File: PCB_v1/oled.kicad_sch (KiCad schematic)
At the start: 17 parts, among them J6 OLED Conn_02x04, SW2 SW_Push, SW3 SW_Push, SW4 SW_Push, SW5 SW_Push, SW6 SW_Push, SW7 SW_Push, U3 SMS05T1G, U4 SMS05T1G

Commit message: added the oscilator
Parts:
- TP3, TP4, TP5, TP6: footprint TestPoint:TestPoint_THTPad_D1.0mm_Drill0.5mm -> TestPoint_THTPad_D0.5mm_Drill0.3mm
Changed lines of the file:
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@@
 	(label "B5"
 		(at 77.47 148.59 0)
+		(fields_autoplaced yes)
 		(effects
 			(font
@@
 	(label "B1"
 		(at 22.86 46.99 0)
+		(fields_autoplaced yes)
 		(effects
 			(font
@@
 	(label "B6"
 		(at 77.47 179.07 0)
+		(fields_autoplaced yes)
 		(effects
 			(font
@@
 	(label "B7"
 		(at 22.86 87.63 0)
+		(fields_autoplaced yes)
 		(effects
 			(font
@@
 	(label "B8"
 		(at 55.88 87.63 0)
+		(fields_autoplaced yes)
 		(effects
 			(font
@@
 	(label "B4"
 		(at 77.47 116.84 0)
+		(fields_autoplaced yes)
 		(effects
 			(font
@@
 	(label "B1"
 		(at 77.47 33.02 0)
+		(fields_autoplaced yes)
 		(effects
 			(font
@@
 	(label "B7"
 		(at 187.96 104.14 0)
+		(fields_autoplaced yes)
 		(effects
 			(font
@@
 	(label "B3"
 		(at 77.47 88.9 0)
+		(fields_autoplaced yes)
 		(effects
 			(font
@@
 	(label "B3"
 		(at 55.88 57.15 0)
+		(fields_autoplaced yes)
 		(effects
 			(font
@@
 	(label "B2"
 		(at 77.47 59.69 0)
+		(fields_autoplaced yes)
 		(effects
 			(font
@@
 	(label "B4"
 		(at 22.86 57.15 0)
+		(fields_autoplaced yes)
 		(effects
 			(font
@@
 	(label "B6"
 		(at 55.88 77.47 0)
+		(fields_autoplaced yes)
 		(effects
 			(font
@@
 	(label "B2"
 		(at 55.88 46.99 0)
+		(fields_autoplaced yes)
 		(effects
 			(font
@@
 	(label "B5"
 		(at 22.86 77.47 0)
+		(fields_autoplaced yes)
 		(effects
 			(font
@@
 	(label "B8"
 		(at 189.23 139.7 0)
+		(fields_autoplaced yes)
 		(effects
 			(font
@@
 		(shape output)
 		(at 104.14 116.84 0)
+		(fields_autoplaced yes)
 		(effects
 			(font
@@
 		(shape input)
 		(at 149.86 49.53 0)
+		(fields_autoplaced yes)
 		(effects
 			(font
@@
 		(shape input)
 		(at 137.16 41.91 180)
+		(fields_autoplaced yes)
 		(effects
 			(font
@@
 		(shape input)
 		(at 137.16 46.99 180)
+		(fields_autoplaced yes)
 		(effects
 			(font
@@
 		(shape output)
 		(at 104.14 59.69 0)
+		(fields_autoplaced yes)
 		(effects
 			(font
@@
 		(shape input)
 		(at 149.86 41.91 0)
+		(fields_autoplaced yes)
 		(effects
 			(font
@@
 		(shape input)
 		(at 149.86 44.45 0)
+		(fields_autoplaced yes)
 		(effects
 			(font
@@
 		(shape output)
 		(at 104.14 88.9 0)
+		(fields_autoplaced yes)
 		(effects
 			(font
@@
 		(shape output)
 		(at 104.14 179.07 0)
+		(fields_autoplaced yes)
 		(effects
 			(font
@@
 		(shape input)
 		(at 137.16 49.53 180)
+		(fields_autoplaced yes)
 		(effects
 			(font
@@
 		(shape input)
 		(at 154.94 73.66 0)
+		(fields_autoplaced yes)
 		(effects
 			(font
@@
 		(shape input)
 		(at 137.16 44.45 180)
+		(fields_autoplaced yes)
 		(effects
 			(font
@@
 		(shape output)
 		(at 104.14 148.59 0)
+		(fields_autoplaced yes)
 		(effects
 			(font
@@
 		(shape input)
 		(at 134.62 73.66 0)
+		(fields_autoplaced yes)
 		(effects
 			(font
@@
 		(shape output)
 		(at 104.14 33.02 0)
+		(fields_autoplaced yes)
 		(effects
 			(font
@@
 		(shape input)
 		(at 149.86 46.99 0)
+		(fields_autoplaced yes)
 		(effects
 			(font
@@
 			)
 		)
-		(property "Footprint" "TestPoint:TestPoint_THTPad_D1.0mm_Drill0.5mm"
+		(property "Footprint" "TestPoint_THTPad_D0.5mm_Drill0.3mm"
 			(at 194.31 144.78 0)
 			(effects
@@
 			)
 		)
-		(property "Footprint" "TestPoint:TestPoint_THTPad_D1.0mm_Drill0.5mm"
+		(property "Footprint" "TestPoint_THTPad_D0.5mm_Drill0.3mm"
 			(at 161.29 134.62 0)
 			(effects
@@
 			)
 		)
-		(property "Footprint" "TestPoint:TestPoint_THTPad_D1.0mm_Drill0.5mm"
+		(property "Footprint" "TestPoint_THTPad_D0.5mm_Drill0.3mm"
 			(at 161.29 100.33 0)
 			(effects
@@
 			)
 		)
-		(property "Footprint" "TestPoint:TestPoint_THTPad_D1.0mm_Drill0.5mm"
+		(property "Footprint" "TestPoint_THTPad_D0.5mm_Drill0.3mm"
 			(at 193.04 109.22 0)
 			(effects

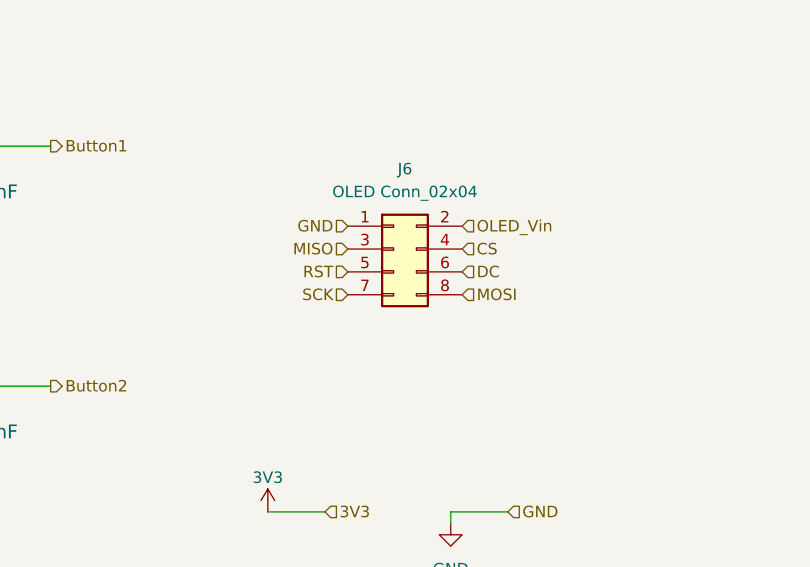
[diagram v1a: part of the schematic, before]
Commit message: push for jtag fix
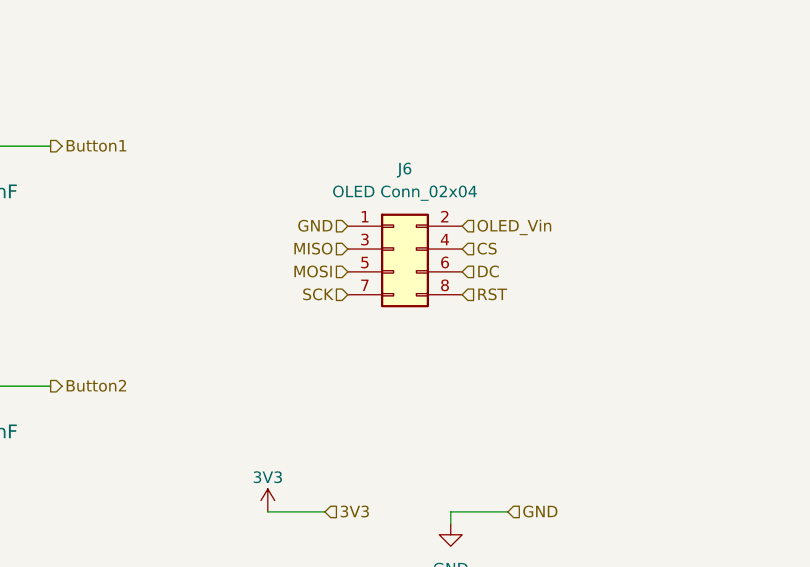
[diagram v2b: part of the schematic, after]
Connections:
- net MOSI: now also J6.5 (Pin_5); no longer J6.8 (Pin_8)
- net RST: now also J6.8 (Pin_8); no longer J6.5 (Pin_5)
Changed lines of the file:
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@@
 	(label "B5"
 		(at 77.47 148.59 0)
-		(fields_autoplaced yes)
 		(effects
 			(font
@@
 	(label "B1"
 		(at 22.86 46.99 0)
-		(fields_autoplaced yes)
 		(effects
 			(font
@@
 	(label "B6"
 		(at 77.47 179.07 0)
-		(fields_autoplaced yes)
 		(effects
 			(font
@@
 	(label "B7"
 		(at 22.86 87.63 0)
-		(fields_autoplaced yes)
 		(effects
 			(font
@@
 	(label "B8"
 		(at 55.88 87.63 0)
-		(fields_autoplaced yes)
 		(effects
 			(font
@@
 	(label "B4"
 		(at 77.47 116.84 0)
-		(fields_autoplaced yes)
 		(effects
 			(font
@@
 	(label "B1"
 		(at 77.47 33.02 0)
-		(fields_autoplaced yes)
 		(effects
 			(font
@@
 	(label "B7"
 		(at 187.96 104.14 0)
-		(fields_autoplaced yes)
 		(effects
 			(font
@@
 	(label "B3"
 		(at 77.47 88.9 0)
-		(fields_autoplaced yes)
 		(effects
 			(font
@@
 	(label "B3"
 		(at 55.88 57.15 0)
-		(fields_autoplaced yes)
 		(effects
 			(font
@@
 	(label "B2"
 		(at 77.47 59.69 0)
-		(fields_autoplaced yes)
 		(effects
 			(font
@@
 	(label "B4"
 		(at 22.86 57.15 0)
-		(fields_autoplaced yes)
 		(effects
 			(font
@@
 	(label "B6"
 		(at 55.88 77.47 0)
-		(fields_autoplaced yes)
 		(effects
 			(font
@@
 	(label "B2"
 		(at 55.88 46.99 0)
-		(fields_autoplaced yes)
 		(effects
 			(font
@@
 	(label "B5"
 		(at 22.86 77.47 0)
-		(fields_autoplaced yes)
 		(effects
 			(font
@@
 	(label "B8"
 		(at 189.23 139.7 0)
-		(fields_autoplaced yes)
 		(effects
 			(font
@@
 		(shape output)
 		(at 104.14 116.84 0)
-		(fields_autoplaced yes)
 		(effects
 			(font
@@
 	(hierarchical_label "MOSI"
 		(shape input)
+		(at 137.16 46.99 180)
+		(effects
+			(font
+				(size 1.27 1.27)
+			)
+			(justify right)
+		)
+	)
+	(hierarchical_label "GND"
+		(shape input)
+		(at 137.16 41.91 180)
+		(effects
+			(font
+				(size 1.27 1.27)
+			)
+			(justify right)
+		)
+	)
+	(hierarchical_label "RST"
+		(shape input)
 		(at 149.86 49.53 0)
-		(fields_autoplaced yes)
-		(effects
-			(font
-				(size 1.27 1.27)
-			)
-			(justify left)
+		(effects
+			(font
+				(size 1.27 1.27)
+			)
+			(justify left)
+		)
+	)
+	(hierarchical_label "Button2"
+		(shape output)
+		(at 104.14 59.69 0)
+		(effects
+			(font
+				(size 1.27 1.27)
+			)
+			(justify left)
+		)
+	)
+	(hierarchical_label "OLED_Vin"
+		(shape input)
+		(at 149.86 41.91 0)
+		(effects
+			(font
+				(size 1.27 1.27)
+			)
+			(justify left)
+		)
+	)
+	(hierarchical_label "CS"
+		(shape input)
+		(at 149.86 44.45 0)
+		(effects
+			(font
+				(size 1.27 1.27)
+			)
+			(justify left)
+		)
+	)
+	(hierarchical_label "Button3"
+		(shape output)
+		(at 104.14 88.9 0)
+		(effects
+			(font
+				(size 1.27 1.27)
+			)
+			(justify left)
+		)
+	)
+	(hierarchical_label "Button6"
+		(shape output)
+		(at 104.14 179.07 0)
+		(effects
+			(font
+				(size 1.27 1.27)
+			)
+			(justify left)
+		)
+	)
+	(hierarchical_label "SCK"
+		(shape input)
+		(at 137.16 49.53 180)
+		(effects
+			(font
+				(size 1.27 1.27)
+			)
+			(justify right)
 		)
 	)
 	(hierarchical_label "GND"
 		(shape input)
-		(at 137.16 41.91 180)
-		(fields_autoplaced yes)
-		(effects
-			(font
-				(size 1.27 1.27)
-			)
-			(justify right)
-		)
-	)
-	(hierarchical_label "RST"
-		(shape input)
-		(at 137.16 46.99 180)
-		(fields_autoplaced yes)
-		(effects
-			(font
-				(size 1.27 1.27)
-			)
-			(justify right)
-		)
-	)
-	(hierarchical_label "Button2"
-		(shape output)
-		(at 104.14 59.69 0)
-		(fields_autoplaced yes)
-		(effects
-			(font
-				(size 1.27 1.27)
-			)
-			(justify left)
-		)
-	)
-	(hierarchical_label "OLED_Vin"
-		(shape input)
-		(at 149.86 41.91 0)
-		(fields_autoplaced yes)
-		(effects
-			(font
-				(size 1.27 1.27)
-			)
-			(justify left)
-		)
-	)
-	(hierarchical_label "CS"
-		(shape input)
-		(at 149.86 44.45 0)
-		(fields_autoplaced yes)
-		(effects
-			(font
-				(size 1.27 1.27)
-			)
-			(justify left)
-		)
-	)
-	(hierarchical_label "Button3"
-		(shape output)
-		(at 104.14 88.9 0)
-		(fields_autoplaced yes)
-		(effects
-			(font
-				(size 1.27 1.27)
-			)
-			(justify left)
-		)
-	)
-	(hierarchical_label "Button6"
-		(shape output)
-		(at 104.14 179.07 0)
-		(fields_autoplaced yes)
-		(effects
-			(font
-				(size 1.27 1.27)
-			)
-			(justify left)
-		)
-	)
-	(hierarchical_label "SCK"
-		(shape input)
-		(at 137.16 49.53 180)
-		(fields_autoplaced yes)
-		(effects
-			(font
-				(size 1.27 1.27)
-			)
-			(justify right)
-		)
-	)
-	(hierarchical_label "GND"
-		(shape input)
 		(at 154.94 73.66 0)
-		(fields_autoplaced yes)
 		(effects
 			(font
@@
 		(shape input)
 		(at 137.16 44.45 180)
-		(fields_autoplaced yes)
 		(effects
 			(font
@@
 		(shape output)
 		(at 104.14 148.59 0)
-		(fields_autoplaced yes)
 		(effects
 			(font
@@
 		(shape input)
 		(at 134.62 73.66 0)
-		(fields_autoplaced yes)
 		(effects
 			(font
@@
 		(shape output)
 		(at 104.14 33.02 0)
-		(fields_autoplaced yes)
 		(effects
 			(font
@@
 		(shape input)
 		(at 149.86 46.99 0)
-		(fields_autoplaced yes)
-		(effects
-			(font
+		(effects
+			(font

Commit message: before major move
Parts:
- TP3, TP4, TP5, TP6: footprint TestPoint_THTPad_D0.5mm_Drill0.3mm -> TestPoint_THTPad_D0.8mm_Drill0.4mm
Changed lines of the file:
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@@
 			)
 		)
-		(property "Footprint" "TestPoint_THTPad_D0.5mm_Drill0.3mm"
+		(property "Footprint" "TestPoint_THTPad_D0.8mm_Drill0.4mm"
 			(at 194.31 144.78 0)
 			(effects
@@
 			)
 		)
-		(property "Footprint" "TestPoint_THTPad_D0.5mm_Drill0.3mm"
+		(property "Footprint" "TestPoint_THTPad_D0.8mm_Drill0.4mm"
 			(at 161.29 134.62 0)
 			(effects
@@
 			)
 		)
-		(property "Footprint" "TestPoint_THTPad_D0.5mm_Drill0.3mm"
+		(property "Footprint" "TestPoint_THTPad_D0.8mm_Drill0.4mm"
 			(at 161.29 100.33 0)
 			(effects
@@
 			)
 		)
-		(property "Footprint" "TestPoint_THTPad_D0.5mm_Drill0.3mm"
+		(property "Footprint" "TestPoint_THTPad_D0.8mm_Drill0.4mm"
 			(at 193.04 109.22 0)
 			(effects

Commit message: Placement done
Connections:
- net B1: now also U3.6; no longer U3.4
- net B2: now also U3.4; no longer U3.3
- net B3: now also U3.3; no longer U3.1
- net B4: now also U3.1; no longer U3.6
- net CS: now also J6.7 (Pin_7); no longer J6.4 (Pin_4)
- net GND: now also J6.2 (Pin_2); no longer J6.1 (Pin_1)
- net MOSI: now also J6.1 (Pin_1); no longer J6.5 (Pin_5)
- net OLED_Vin: now also J6.4 (Pin_4); no longer J6.2 (Pin_2)
- net SCK: now also J6.5 (Pin_5); no longer J6.7 (Pin_7)
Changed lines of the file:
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@@
+	(wire
+		(pts
+			(xy 151.13 46.99) (xy 149.86 46.99)
+		)
+		(stroke
+			(width 0)
+			(type default)
+		)
+	)
 	(wire
 		(pts
@@
 	(wire
 		(pts
+			(xy 19.05 57.15) (xy 22.86 57.15)
+		)
+		(stroke
+			(width 0)
+			(type default)
+		)
+	)
+	(wire
+		(pts
 			(xy 77.47 148.59) (xy 80.01 148.59)
 		)
@@
 	(wire
 		(pts
+			(xy 57.15 46.99) (xy 55.88 46.99)
+		)
+		(stroke
+			(width 0)
+			(type default)
+		)
+	)
+	(wire
+		(pts
+			(xy 151.13 44.45) (xy 149.86 44.45)
+		)
+		(stroke
+			(width 0)
+			(type default)
+		)
+	)
+	(wire
+		(pts
 			(xy 87.63 33.02) (xy 90.17 33.02)
 		)
@@
 	(wire
 		(pts
+			(xy 135.89 46.99) (xy 137.16 46.99)
+		)
+		(stroke
+			(width 0)
+			(type default)
+		)
+	)
+	(wire
+		(pts
 			(xy 58.42 82.55) (xy 55.88 82.55)
 		)
@@
 	(wire
 		(pts
+			(xy 151.13 49.53) (xy 149.86 49.53)
+		)
+		(stroke
+			(width 0)
+			(type default)
+		)
+	)
+	(wire
+		(pts
 			(xy 64.77 148.59) (xy 67.31 148.59)
 		)
@@
 	(wire
 		(pts
+			(xy 135.89 44.45) (xy 137.16 44.45)
+		)
+		(stroke
+			(width 0)
+			(type default)
+		)
+	)
+	(wire
+		(pts
+			(xy 151.13 41.91) (xy 149.86 41.91)
+		)
+		(stroke
+			(width 0)
+			(type default)
+		)
+	)
+	(wire
+		(pts
 			(xy 64.77 91.44) (xy 64.77 88.9)
 		)
@@
 	(wire
 		(pts
+			(xy 135.89 49.53) (xy 137.16 49.53)
+		)
+		(stroke
+			(width 0)
+			(type default)
+		)
+	)
+	(wire
+		(pts
 			(xy 64.77 179.07) (xy 67.31 179.07)
 		)
@@
 	(wire
 		(pts
+			(xy 57.15 57.15) (xy 55.88 57.15)
+		)
+		(stroke
+			(width 0)
+			(type default)
+		)
+	)
+	(wire
+		(pts
 			(xy 179.07 105.41) (xy 179.07 107.95)
+		)
+		(stroke
+			(width 0)
+			(type default)
+		)
+	)
+	(wire
+		(pts
+			(xy 135.89 41.91) (xy 137.16 41.91)
 		)
 		(stroke
@@
 		)
 	)
-	(label "B1"
-		(at 22.86 46.99 0)
-		(effects
-			(font
-				(size 1.27 1.27)
-			)
-			(justify left bottom)
-		)
-	)
 	(label "B6"
 		(at 77.47 179.07 0)
@@
 	)
 	(label "B1"
+		(at 19.05 57.15 0)
+		(effects
+			(font
+				(size 1.27 1.27)
+			)
+			(justify left bottom)
+		)
+	)
+	(label "B1"
 		(at 77.47 33.02 0)
 		(effects
@@
 		)
 	)
+	(label "B4"
+		(at 57.15 57.15 0)
+		(effects
+			(font
+				(size 1.27 1.27)
+			)
+			(justify left bottom)
+		)
+	)
 	(label "B3"
 		(at 77.47 88.9 0)
@@
 		)
 	)
-	(label "B3"
-		(at 55.88 57.15 0)
-		(effects
-			(font
-				(size 1.27 1.27)
-			)
-			(justify left bottom)
-		)
-	)
 	(label "B2"
 		(at 77.47 59.69 0)
@@
 		)
 	)
-	(label "B4"
-		(at 22.86 57.15 0)
-		(effects
-			(font
-				(size 1.27 1.27)
-			)
-			(justify left bottom)
-		)
-	)
 	(label "B6"
 		(at 55.88 77.47 0)
@@
 	)
 	(label "B2"
-		(at 55.88 46.99 0)
+		(at 22.86 46.99 0)
+		(effects
+			(font
+				(size 1.27 1.27)
+			)
+			(justify left bottom)
+		)
+	)
+	(label "B3"
+		(at 57.15 46.99 0)
 		(effects
 			(font
@@
 			)
 			(justify left bottom)
+		)
+	)
+	(hierarchical_label "MOSI"
+		(shape input)
+		(at 135.89 41.91 180)
+		(effects
+			(font
+				(size 1.27 1.27)
+			)
+			(justify right)
 		)
 	)
@@
 		)
 	)
-	(hierarchical_label "MOSI"
-		(shape input)
-		(at 137.16 46.99 180)
+	(hierarchical_label "CS"
+		(shape input)
+		(at 135.89 49.53 180)
 		(effects
 			(font
@@
 		)
 	)
-	(hierarchical_label "GND"
-		(shape input)
-		(at 137.16 41.91 180)
-		(effects
-			(font
-				(size 1.27 1.27)
-			)
-			(justify right)
-		)
-	)
-	(hierarchical_label "RST"
-		(shape input)
-		(at 149.86 49.53 0)
+	(hierarchical_label "DC"
+		(shape input)
+		(at 151.13 46.99 0)
 		(effects
 			(font
@@
 		)
 	)
-	(hierarchical_label "OLED_Vin"
-		(shape input)
-		(at 149.86 41.91 0)
-		(effects
-			(font
-				(size 1.27 1.27)
-			)
-			(justify left)
-		)
-	)
-	(hierarchical_label "CS"
-		(shape input)
-		(at 149.86 44.45 0)
+	(hierarchical_label "SCK"
+		(shape input)
+		(at 135.89 46.99 180)
+		(effects
+			(font
+				(size 1.27 1.27)
+			)
+			(justify right)
+		)
+	)
+	(hierarchical_label "RST"
+		(shape input)
+		(at 151.13 49.53 0)
+		(effects
+			(font
+				(size 1.27 1.27)
+			)
+			(justify left)
+		)
+	)
+	(hierarchical_label "GND"
+		(shape input)
+		(at 151.13 41.91 0)
 		(effects
 			(font
@@
 		)
 	)
-	(hierarchical_label "SCK"
-		(shape input)
-		(at 137.16 49.53 180)
-		(effects
-			(font
-				(size 1.27 1.27)
-			)
-			(justify right)
-		)
-	)
 	(hierarchical_label "GND"
 		(shape input)
@@
 		)
 	)
-	(hierarchical_label "MISO"
-		(shape input)
-		(at 137.16 44.45 180)
-		(effects
-			(font
-				(size 1.27 1.27)
-			)
-			(justify right)
+	(hierarchical_label "OLED_Vin"
+		(shape input)
+		(at 151.13 44.45 0)
+		(effects
+			(font
+				(size 1.27 1.27)
+			)
+			(justify left)
 		)
 	)
@@
 		)
 	)
-	(hierarchical_label "DC"
-		(shape input)
-		(at 149.86 46.99 0)
-		(effects
-			(font
-				(size 1.27 1.27)
-			)
-			(justify left)
-		)
-	)
+	(hierarchical_label "MISO"
+		(shape input)
+		(at 135.89 44.45 180)
+		(effects
+			(font
+				(size 1.27 1.27)
+			)
+			(justify right)
+		)
+	)

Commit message: before DRC
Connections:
- net CS: now also J6.8 (Pin_8); no longer J6.7 (Pin_7)
- net RST: now also J6.7 (Pin_7); no longer J6.8 (Pin_8)
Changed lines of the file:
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@@
+	(wire
+		(pts
+			(xy 135.89 49.53) (xy 137.16 49.53)
+		)
+		(stroke
+			(width 0)
+			(type default)
+		)
+	)
 	(wire
 		(pts
@@
 	(wire
 		(pts
+			(xy 64.77 148.59) (xy 67.31 148.59)
+		)
+		(stroke
+			(width 0)
+			(type default)
+		)
+	)
+	(wire
+		(pts
+			(xy 179.07 139.7) (xy 179.07 140.97)
+		)
+		(stroke
+			(width 0)
+			(type default)
+		)
+	)
+	(wire
+		(pts
+			(xy 87.63 148.59) (xy 90.17 148.59)
+		)
+		(stroke
+			(width 0)
+			(type default)
+		)
+	)
+	(wire
+		(pts
+			(xy 161.29 105.41) (xy 167.64 105.41)
+		)
+		(stroke
+			(width 0)
+			(type default)
+		)
+	)
+	(wire
+		(pts
+			(xy 20.32 52.07) (xy 22.86 52.07)
+		)
+		(stroke
+			(width 0)
+			(type default)
+		)
+	)
+	(wire
+		(pts
+			(xy 135.89 44.45) (xy 137.16 44.45)
+		)
+		(stroke
+			(width 0)
+			(type default)
+		)
+	)
+	(wire
+		(pts
+			(xy 151.13 41.91) (xy 149.86 41.91)
+		)
+		(stroke
+			(width 0)
+			(type default)
+		)
+	)
+	(wire
+		(pts
+			(xy 64.77 91.44) (xy 64.77 88.9)
+		)
+		(stroke
+			(width 0)
+			(type default)
+		)
+	)
+	(wire
+		(pts
 			(xy 151.13 49.53) (xy 149.86 49.53)
 		)
@@
 	(wire
 		(pts
-			(xy 64.77 148.59) (xy 67.31 148.59)
-		)
-		(stroke
-			(width 0)
-			(type default)
-		)
-	)
-	(wire
-		(pts
-			(xy 179.07 139.7) (xy 179.07 140.97)
-		)
-		(stroke
-			(width 0)
-			(type default)
-		)
-	)
-	(wire
-		(pts
-			(xy 87.63 148.59) (xy 90.17 148.59)
-		)
-		(stroke
-			(width 0)
-			(type default)
-		)
-	)
-	(wire
-		(pts
-			(xy 161.29 105.41) (xy 167.64 105.41)
-		)
-		(stroke
-			(width 0)
-			(type default)
-		)
-	)
-	(wire
-		(pts
-			(xy 20.32 52.07) (xy 22.86 52.07)
-		)
-		(stroke
-			(width 0)
-			(type default)
-		)
-	)
-	(wire
-		(pts
-			(xy 135.89 44.45) (xy 137.16 44.45)
-		)
-		(stroke
-			(width 0)
-			(type default)
-		)
-	)
-	(wire
-		(pts
-			(xy 151.13 41.91) (xy 149.86 41.91)
-		)
-		(stroke
-			(width 0)
-			(type default)
-		)
-	)
-	(wire
-		(pts
-			(xy 64.77 91.44) (xy 64.77 88.9)
-		)
-		(stroke
-			(width 0)
-			(type default)
-		)
-	)
-	(wire
-		(pts
 			(xy 58.42 52.07) (xy 55.88 52.07)
 		)
@@
 		(pts
 			(xy 90.17 33.02) (xy 104.14 33.02)
-		)
-		(stroke
-			(width 0)
-			(type default)
-		)
-	)
-	(wire
-		(pts
-			(xy 135.89 49.53) (xy 137.16 49.53)
 		)
 		(stroke
@@
 	(hierarchical_label "CS"
 		(shape input)
-		(at 135.89 49.53 180)
-		(effects
-			(font
-				(size 1.27 1.27)
-			)
-			(justify right)
+		(at 151.13 49.53 0)
+		(effects
+			(font
+				(size 1.27 1.27)
+			)
+			(justify left)
 		)
 	)
@@
 	(hierarchical_label "RST"
 		(shape input)
-		(at 151.13 49.53 0)
-		(effects
-			(font
-				(size 1.27 1.27)
-			)
-			(justify left)
-		)
-	)
+		(at 135.89 49.53 180)
+		(effects
+			(font
+				(size 1.27 1.27)
+			)
+			(justify right)
+		)
+	)
